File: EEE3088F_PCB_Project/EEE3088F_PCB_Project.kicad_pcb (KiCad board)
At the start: 2 copper layers, 82 x 72.7 mm, 107 parts, among them IC1 DRV8833PWPR, IC2 DRV8833PWPR, IC3 TPS62067DSGR, IC5 INA219AIDCNR, IC7 TPS61088RHLR, J1 Conn_02x16_Odd_Even, J2 TYPE-C16PIN, J3 Conn_01x02, Q1 AO3400A, Q2 AO3400A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

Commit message: v1.5.1
- made more progress with wiring
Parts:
- moved TP10 21.3 mm to (156.1, 64.5)
- moved U1 19.5 mm to (163.1, 67.6), turned to 180 degrees
- moved TP7 19.4 mm to (177.7, 52.8)
- moved TP34 16.9 mm to (168.7, 79.5)
- moved R29 16.1 mm to (163.1, 64.8)
- moved TP6 14.8 mm to (172.6, 63.2)
- moved TP5 14.6 mm to (177.3, 58.3)
- moved TP28 14.5 mm to (152.4, 69.3), turned to 0 degrees
- moved TP33 12.2 mm to (179.3, 76.5)
- moved TP4 12.1 mm to (159.6, 53.1)
- moved R5 11.2 mm to (151.7, 76.5), turned to 180 degrees
- moved TP36 10.3 mm to (175.8, 83.6), turned to 180 degrees
- moved TP26 10.3 mm to (161.5, 73.4), turned to 180 degrees
- moved TP3 10.3 mm to (167.1, 72.5)
- moved Q6 10.0 mm to (151.9, 72.9)
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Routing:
- net GND: track 162.6 -> 207.0 mm
- net /PWR SWITCH IN: track 59.2 -> 15.3 mm
- net /CC1: track 0.00 -> 30.0 mm
- net /D-: track 0.00 -> 26.7 mm
- net /CC2: track 0.00 -> 15.2 mm
- net /5V OUT: track 31.3 -> 42.3 mm
- net Net-(Q2-D): track 0.00 -> 10.8 mm
- net /MOTOR1_B_OUT: track 0.00 -> 7.39 mm
- net /MOTOR2_A_OUT: track 0.00 -> 6.48 mm
- net Net-(IC1-BISEN): track 0.00 -> 6.43 mm
- net /MOTOR1_A_OUT: track 0.00 -> 5.95 mm
- net Net-(Q2-G): track 0.00 -> 5.62 mm
- net /MOTOR2_B_OUT: track 0.00 -> 4.33 mm
- net /LOAD2: track 0.00 -> 3.86 mm
- net /CTRL_EXT_LOAD2: track 0.00 -> 3.85 mm
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
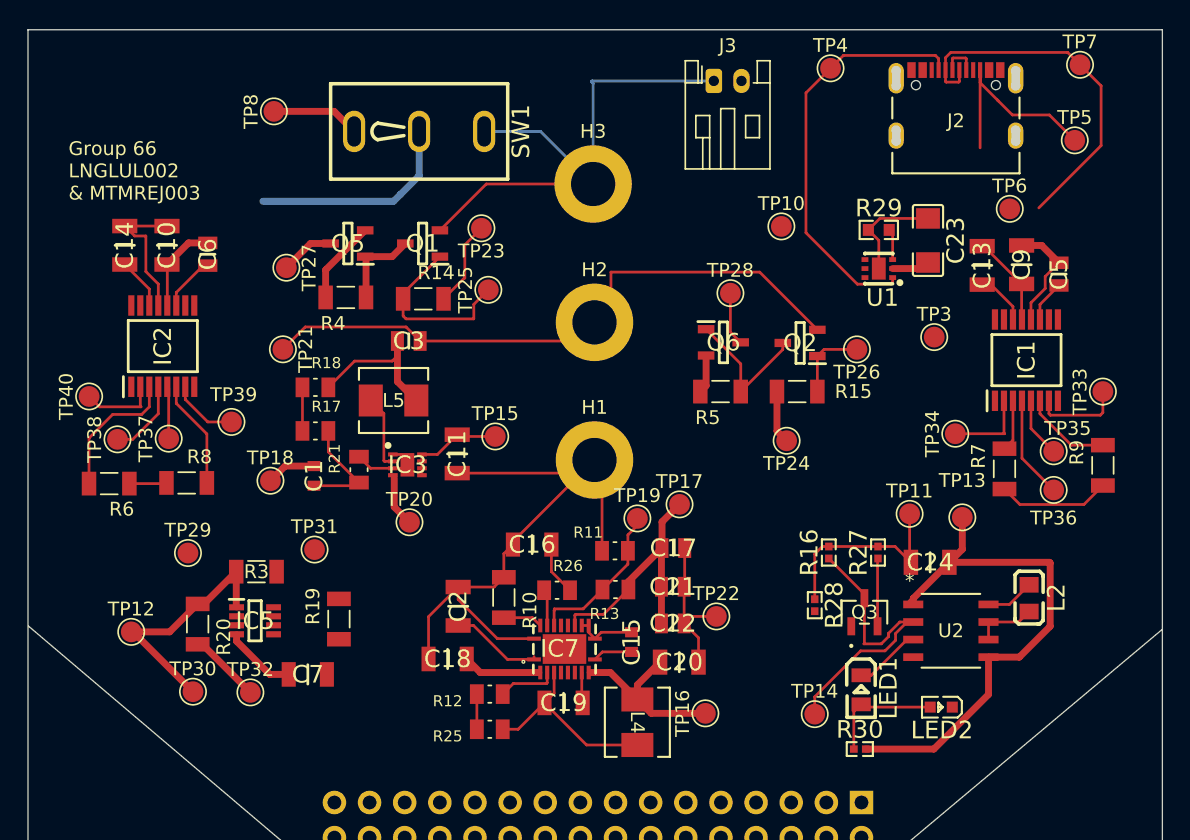
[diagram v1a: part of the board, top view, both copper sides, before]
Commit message: v1.5.2
- resolved 'no connection' issue in battery management
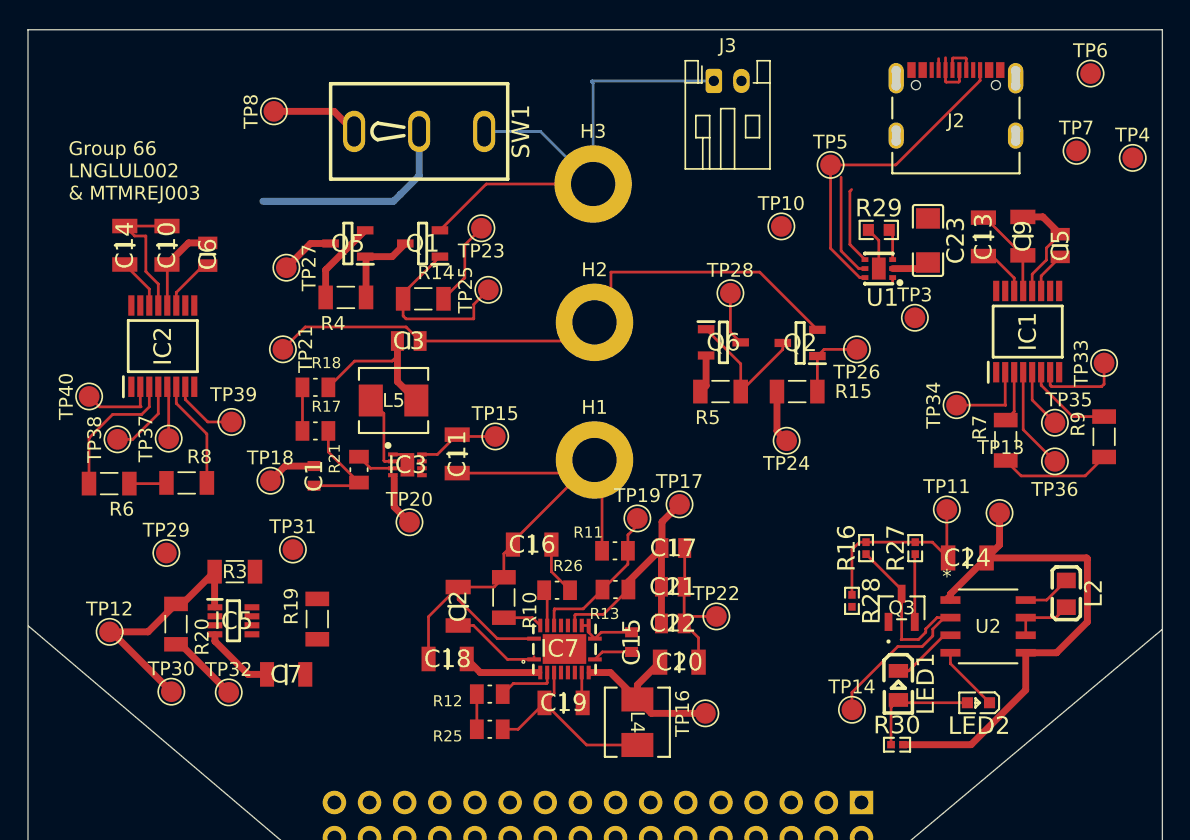
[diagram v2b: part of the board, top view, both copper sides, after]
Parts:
- moved TP4 22.8 mm to (181.5, 59.6)
- moved TP5 17.7 mm to (159.6, 60.1)
- moved TP6 11.4 mm to (178.4, 53.5)
- moved TP7 6.23 mm to (177.4, 59.1)
- moved C24 2.71 mm to (169.5, 88.5)
- moved LED2 2.71 mm to (170.3, 98.9)
- moved Q3 2.71 mm to (164.8, 92.1)
- moved R30 2.71 mm to (164.4, 102.0)
- moved U2 2.71 mm to (171.0, 93.4)
- moved TP13 2.71 mm to (171.9, 85.2)
- moved R28 2.71 mm to (161.2, 91.6)
- moved TP11 2.71 mm to (168.0, 85.0)
- moved L2 2.71 mm to (176.7, 91.1)
- moved LED1 2.71 mm to (164.5, 97.7)
- moved R16 2.71 mm to (162.2, 87.8)
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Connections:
- LED2 pad 1: unconnected-(LED2-K-Pad1) -> Net-(LED2-K)
- U2 pad 4: unconnected-(U2-NCHRG-Pad4) -> Net-(LED2-K)
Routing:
- net /CC1: track 30.0 -> 1.20 mm
- net /D-: track 26.7 -> 11.2 mm
- net /CC2: track 15.2 -> 23.5 mm
- net /D+: track 2.69 -> 8.62 mm
- net Net-(LED2-K): track 0.00 -> 4.79 mm
- net GND: track 207.0 -> 202.4 mm
- net /HV: track 41.5 -> 40.8 mm

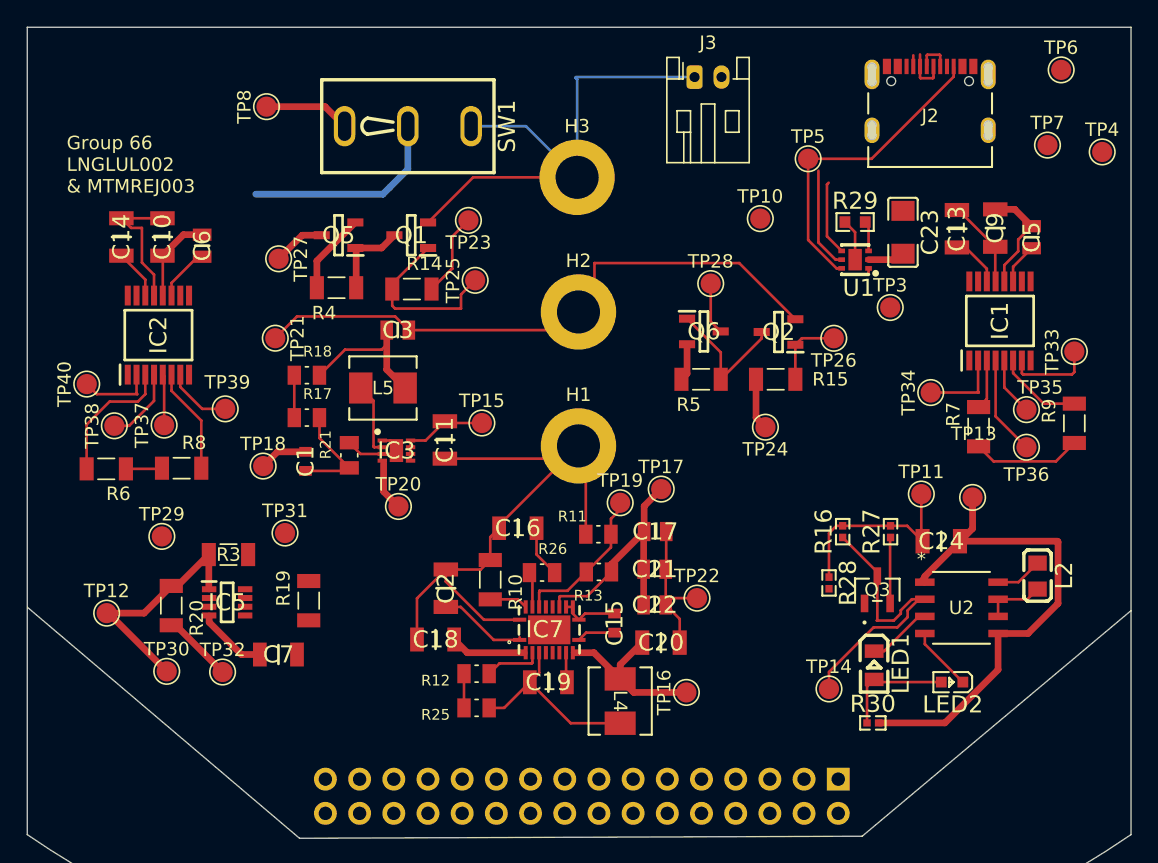
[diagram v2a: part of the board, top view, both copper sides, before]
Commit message: v1.5.3
- started adding vias
- making more progress with wiring
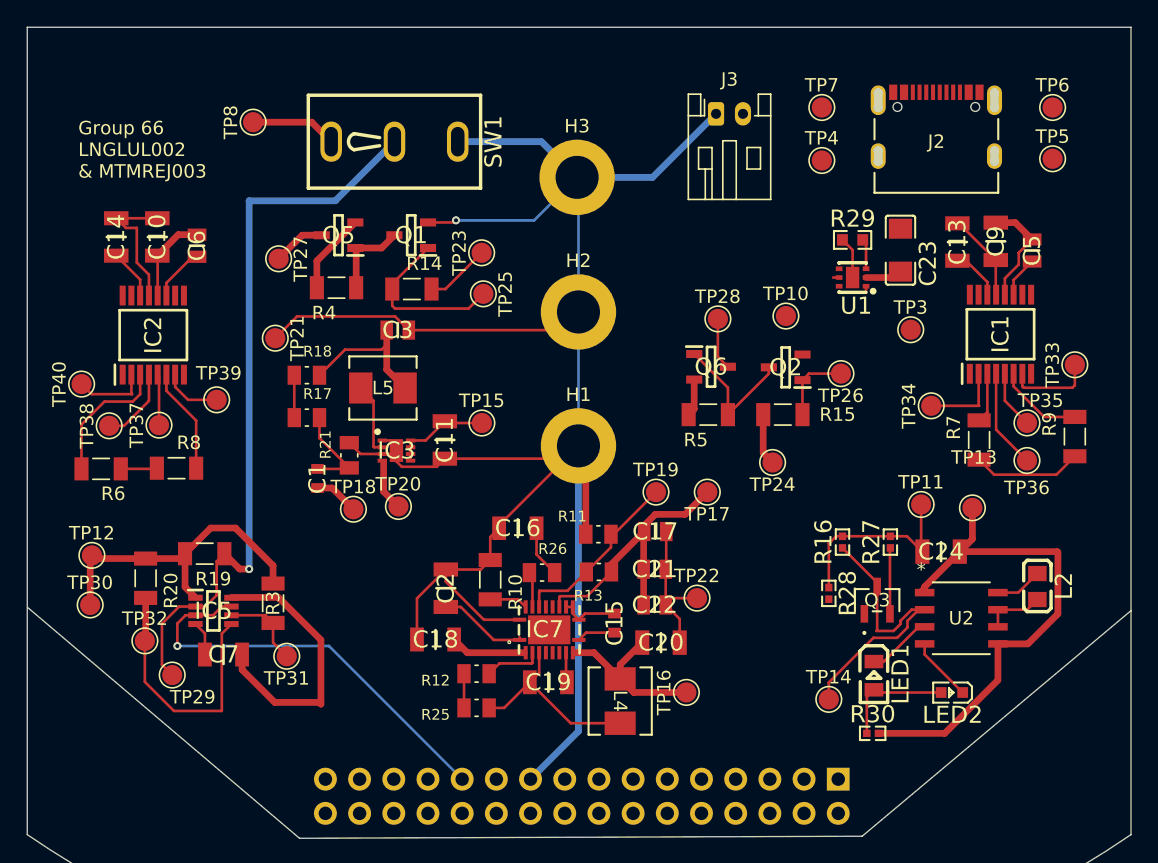
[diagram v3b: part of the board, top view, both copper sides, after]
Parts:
- moved TP4 20.8 mm to (160.7, 60.2)
- moved TP5 18.2 mm to (177.8, 60.1)
- moved TP7 17.0 mm to (160.7, 56.3)
- moved TP29 10.3 mm to (112.4, 98.4), turned to 180 degrees
- moved TP31 9.15 mm to (120.9, 97.0), turned to 180 degrees
- moved R19 8.48 mm to (114.8, 89.4), turned to 180 degrees
- moved TP30 7.53 mm to (106.3, 93.2)
- moved TP10 7.49 mm to (158.0, 71.8)
- moved TP18 7.43 mm to (125.9, 86.1)
- moved TP32 6.22 mm to (110.4, 95.9)
- moved R3 4.90 mm to (119.9, 93.1), turned to -90 degrees
- moved TP12 4.43 mm to (106.4, 89.5)
- moved C7 4.08 mm to (116.2, 96.9)
- moved TP17 3.43 mm to (152.1, 84.8), turned to 180 degrees
- moved J3 3.16 mm to (152.8, 56.7)
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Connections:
- TP29 pad 1: unconnected-(TP29-Pad1) -> /PWR SWITCH IN
- TP31 pad 1: unconnected-(TP31-Pad1) -> /I2C1_SDA
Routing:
- net GND: track 202.4 -> 262.3 mm, vias 0 -> 2
- net /PWR SWITCH IN: track 15.3 -> 54.7 mm, vias 0 -> 1
- net /CC2: track 23.5 -> 0.00 mm
- net /3V3 OUT: track 15.5 -> 36.0 mm
- net /I2C1_SCL: track 5.25 -> 20.0 mm
- net /D-: track 11.2 -> 0.45 mm
- net /D+: track 8.62 -> 0.00 mm
- net /I2C1_SDA: track 0.00 -> 6.22 mm
- net /BATTERY: track 18.8 -> 24.3 mm
- net Net-(IC5-VS): track 5.24 -> 2.56 mm
- net /5V OUT: track 42.3 -> 44.8 mm
- net Net-(IC7-FB): track 11.5 -> 13.5 mm
- net /CTRL_EXT_LOAD1: track 6.26 -> 4.84 mm
- net /CC1: track 1.20 -> 0.38 mm
- net Net-(IC3-FB): track 11.7 -> 11.0 mm
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
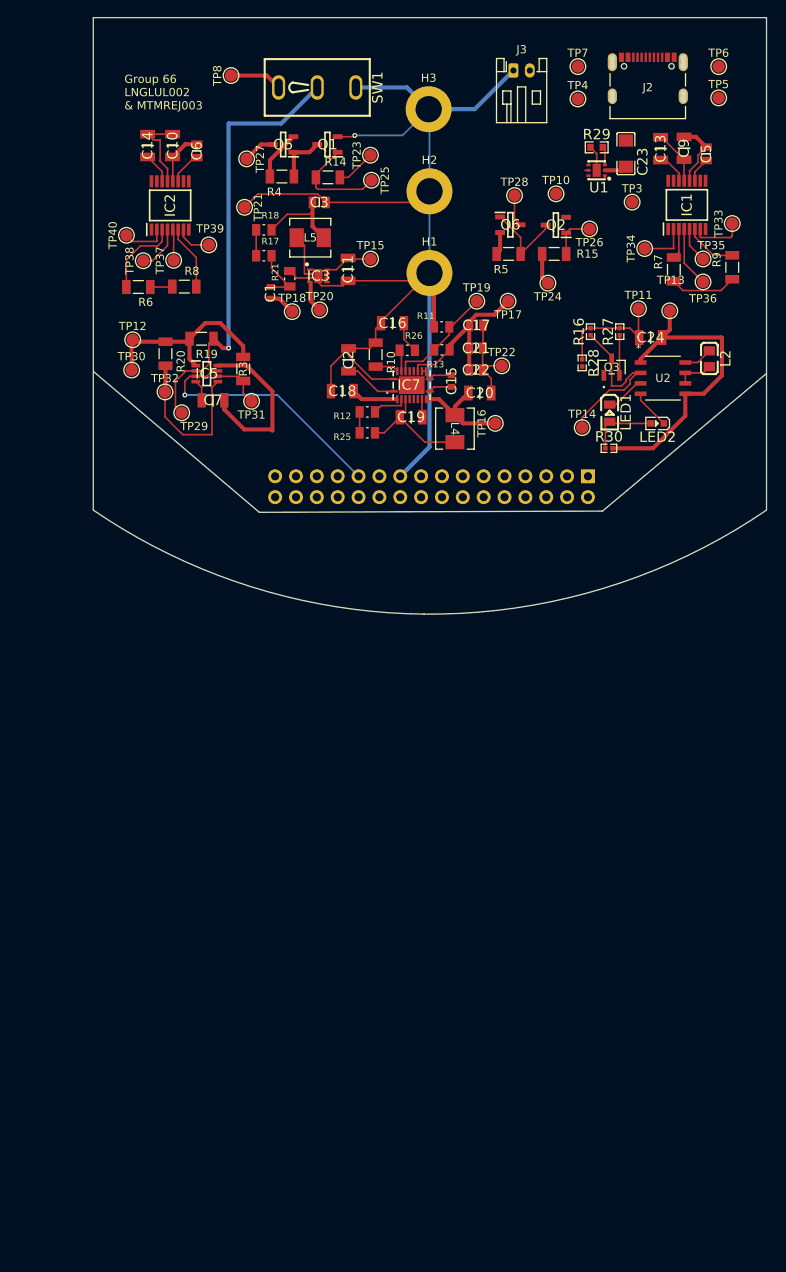
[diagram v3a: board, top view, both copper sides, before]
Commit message: v1.5.4
- need to finish wiring to main connector
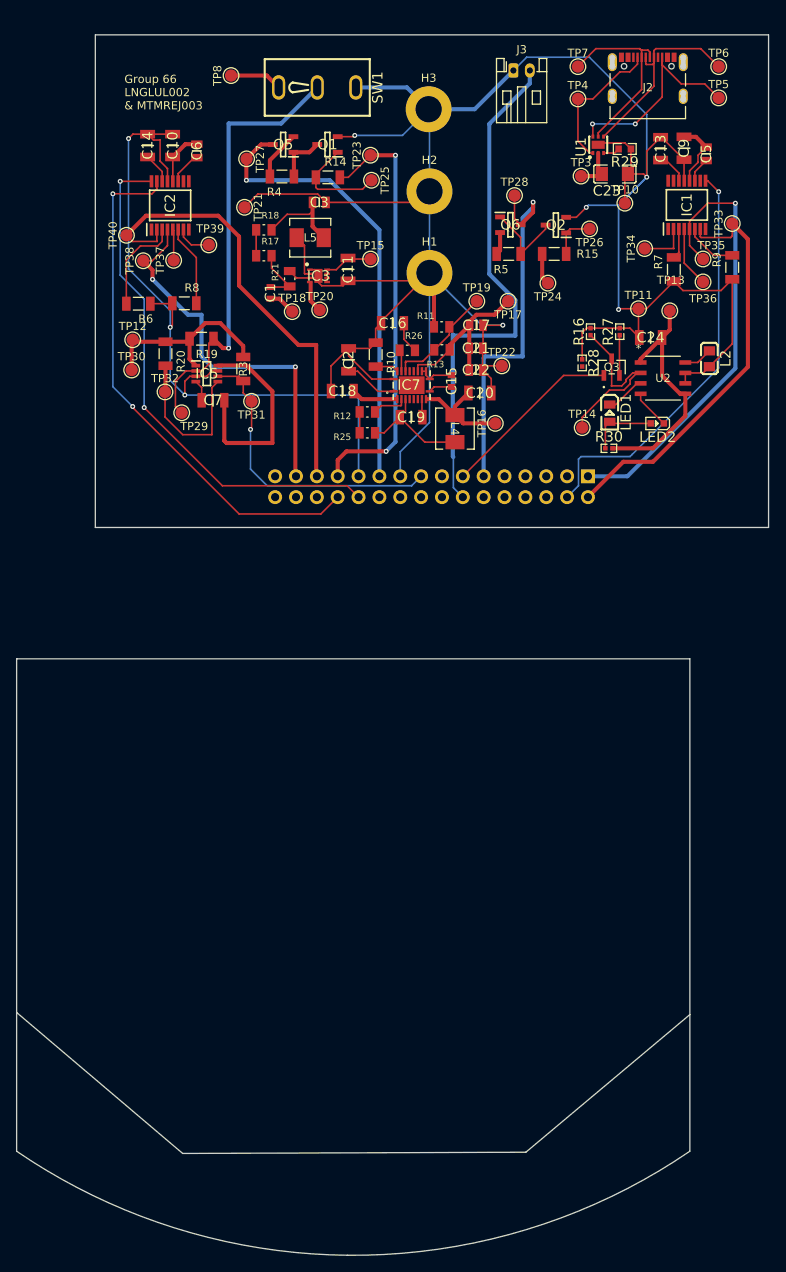
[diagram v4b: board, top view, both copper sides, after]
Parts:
- moved TP10 8.46 mm to (166.4, 72.9)
- moved TP3 6.99 mm to (161.0, 69.6)
- moved R29 3.42 mm to (166.4, 66.3), turned to 180 degrees
- moved U1 3.11 mm to (163.1, 65.8), turned to 90 degrees
- moved C23 2.82 mm to (165.2, 69.3), turned to 180 degrees
- moved R6 2.03 mm to (107.1, 85.1)
- moved R8 2.03 mm to (112.7, 85.1)
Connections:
- Q5 pad 3: /LOAD1 -> /EXT_LOAD1_OUT
- Q6 pad 3: /LOAD2 -> /EXT_LOAD2_OUT
- TP27 pad 1: /LOAD1 -> /EXT_LOAD1_OUT
- TP28 pad 1: /LOAD2 -> /EXT_LOAD2_OUT
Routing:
- net GND: track 262.3 -> 413.9 mm, vias 2 -> 8
- net /MOTOR3_CTRL2: track 0.00 -> 64.8 mm, vias 0 -> 2
- net /BATTERY: track 24.3 -> 87.9 mm
- net /MOTOR3_CTRL1: track 0.00 -> 63.2 mm, vias 0 -> 2
- net /EXT_LOAD1_OUT: track 0.00 -> 55.3 mm, vias 0 -> 1
- net /MOTOR2_B_OUT: track 4.33 -> 55.4 mm, vias 0 -> 1
- net /MOTOR2_CTRL1: track 0.00 -> 50.5 mm, vias 0 -> 1
- net /MOTOR3_A_OUT: track 5.53 -> 55.7 mm
- net /CTRL_EXT_LOAD1: track 4.84 -> 52.7 mm, vias 0 -> 2
- net /EXT_LOAD2_OUT: track 0.00 -> 45.8 mm, vias 0 -> 1
- net /MOTOR2_A_OUT: track 6.48 -> 50.8 mm
- net /MOTOR3_B_OUT: track 5.67 -> 46.5 mm, vias 0 -> 2
- net /I2C1_SDA: track 6.22 -> 36.6 mm, vias 0 -> 1
- net /CC2: track 0.00 -> 25.7 mm, vias 0 -> 2
- net /D+: track 0.00 -> 24.5 mm
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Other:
- board size 82 x 72.7 mm -> 91.6 x 148.6 mm
